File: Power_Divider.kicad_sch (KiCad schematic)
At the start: 28 parts, among them J8 Molex 73251-1153, J9 PIC-S-201F, P10 CONUFL001-SMD-T, P11 CONUFL001-SMD-T, P12 CONUFL001-SMD-T, P9 CONUFL001-SMD-T, U25 QPL9547, U26 RBP-140+

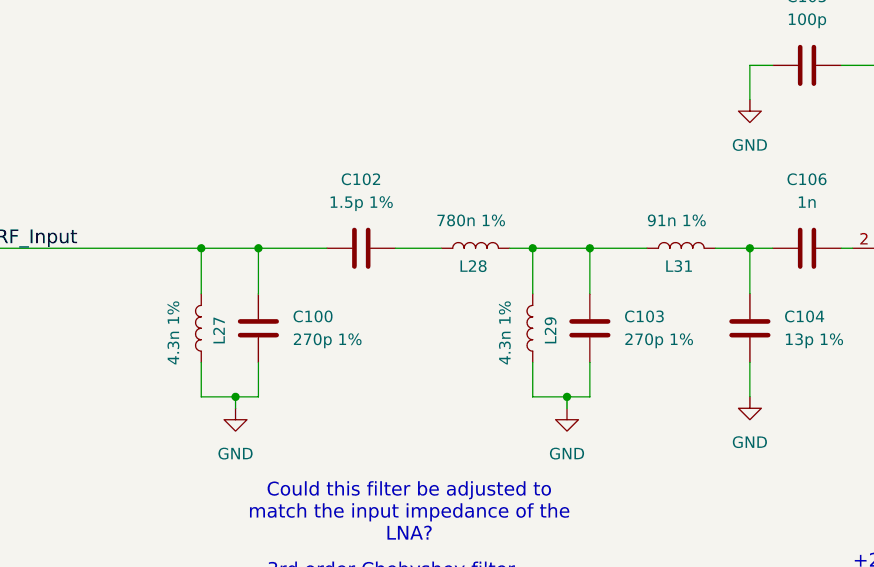
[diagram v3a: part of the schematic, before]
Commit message: More work on the LNA
Rework the filter a bit, rework the layout.

Signed-off-by: Corey Minyard <corey@minyard.net>
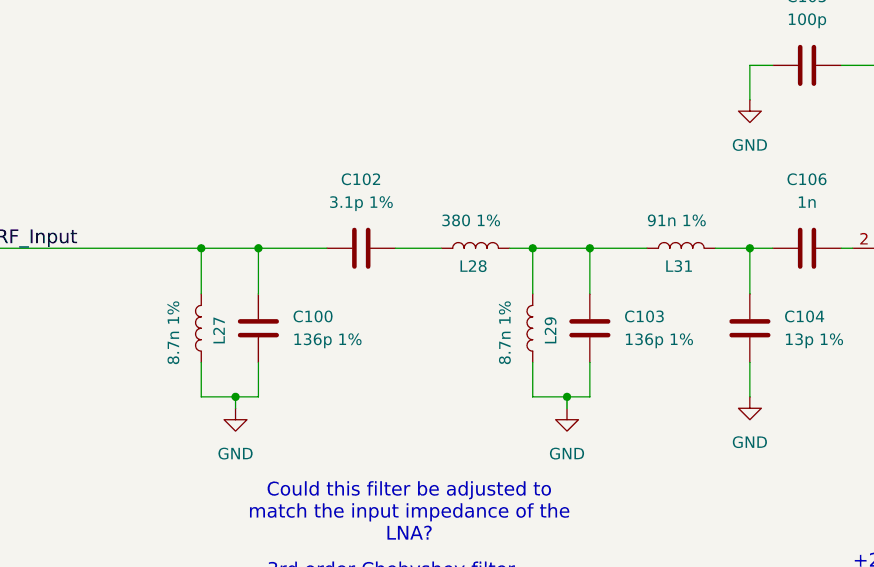
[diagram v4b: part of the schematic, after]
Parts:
- C100, C103: value 270p 1% -> 136p 1%
- C102: value 1.5p 1% -> 3.1p 1%
- L27, L29: value 4.3n 1% -> 8.7n 1%
- L28: value 780n 1% -> 380 1%
- L31: footprint Inductor_SMD:L_0402_1005Metric_Pad0.77x0.64mm_HandSolder -> Inductor_SMD:L_0603_1608Metric_Pad1.05x0.95mm_HandSolder
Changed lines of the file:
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@@
 			)
 		)
-		(property "Footprint" "Inductor_SMD:L_0402_1005Metric_Pad0.77x0.64mm_HandSolder"
+		(property "Footprint" "Inductor_SMD:L_0603_1608Metric_Pad1.05x0.95mm_HandSolder"
 			(at 134.62 143.51 0)
 			(effects
@@
 			)
 		)
-		(property "Value" "270p 1%"
+		(property "Value" "136p 1%"
 			(at 91.44 153.6699 0)
 			(effects
@@
 			)
 		)
-		(property "Value" "4.3n 1%"
+		(property "Value" "8.7n 1%"
 			(at 78.232 152.908 90)
 			(effects
@@
 			)
 		)
-		(property "Value" "780n 1%"
+		(property "Value" "380 1%"
 			(at 111.252 140.462 90)
 			(effects
@@
 			)
 		)
-		(property "Value" "4.3n 1%"
+		(property "Value" "8.7n 1%"
 			(at 115.062 152.908 90)
 			(effects
@@
 			)
 		)
-		(property "Value" "1.5p 1%"
+		(property "Value" "3.1p 1%"
 			(at 99.06 138.43 90)
 			(effects
@@
 			)
 		)
-		(property "Value" "270p 1%"
+		(property "Value" "136p 1%"
 			(at 128.27 153.6699 0)
 			(effects

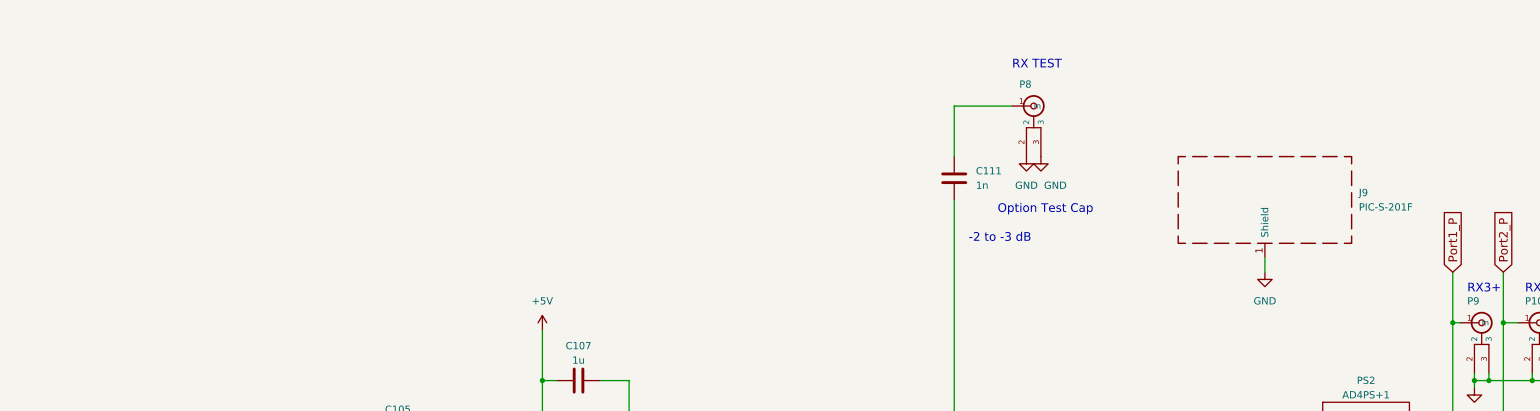
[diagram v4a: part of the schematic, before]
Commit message: Change to aluminum shielding
Signed-off-by: Corey Minyard <corey@minyard.net>
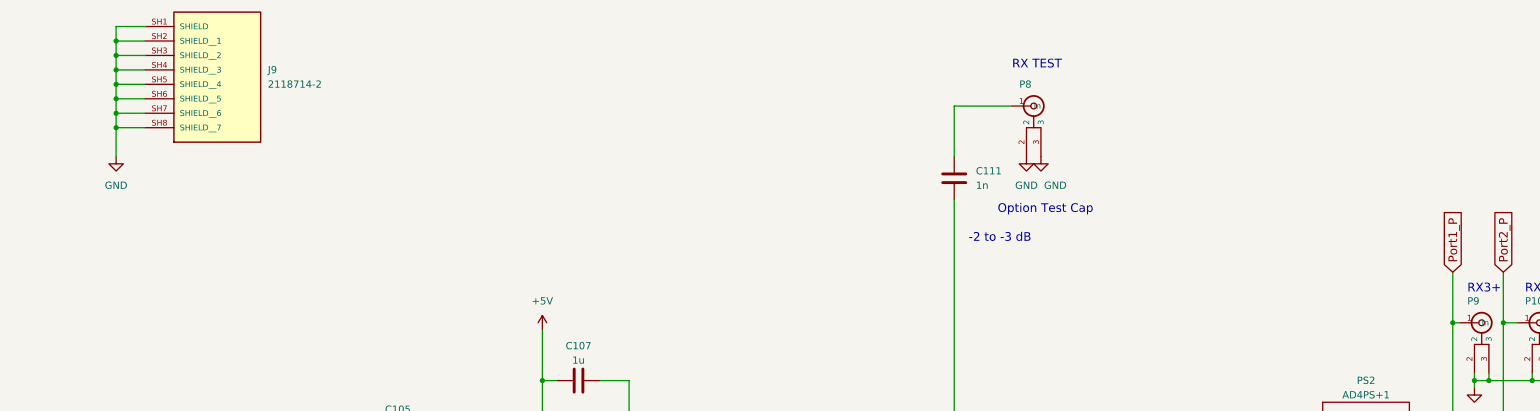
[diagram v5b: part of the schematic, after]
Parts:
- removed J9: PIC-S-201F, PacSatDev_misc:RF_SHIELD_PIC_S_101, symbol Device:RFShield_OnePiece
- added J9: 2118714-2, PacSatDev_misc:TE_2118714-2, symbol PACSAT_DEV_misc:2118714-2
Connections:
- net GND: now also J9.SH1 (SHIELD), J9.SH2 (SHIELD__1), J9.SH3 (SHIELD__2), J9.SH4 (SHIELD__3), J9.SH5 (SHIELD__4), J9.SH6 (SHIELD__5), J9.SH7 (SHIELD__6), J9.SH8 (SHIELD__7)

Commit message: More shield work
Signed-off-by: Corey Minyard <corey@minyard.net>
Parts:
- L28: value 380 1% -> 380n 1%
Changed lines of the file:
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@@
 	(text "3rd order Chebyshev filter\nConventional Shunt First\nPassband 140-152MHz\n.1db ripple in passband\n"
 		(exclude_from_sim no)
-		(at 102.362 183.134 0)
+		(at 101.092 127.254 0)
 		(effects
 			(font
@@
 			)
 		)
-		(property "Value" "380 1%"
+		(property "Value" "380n 1%"
 			(at 111.252 140.462 90)
 			(effects

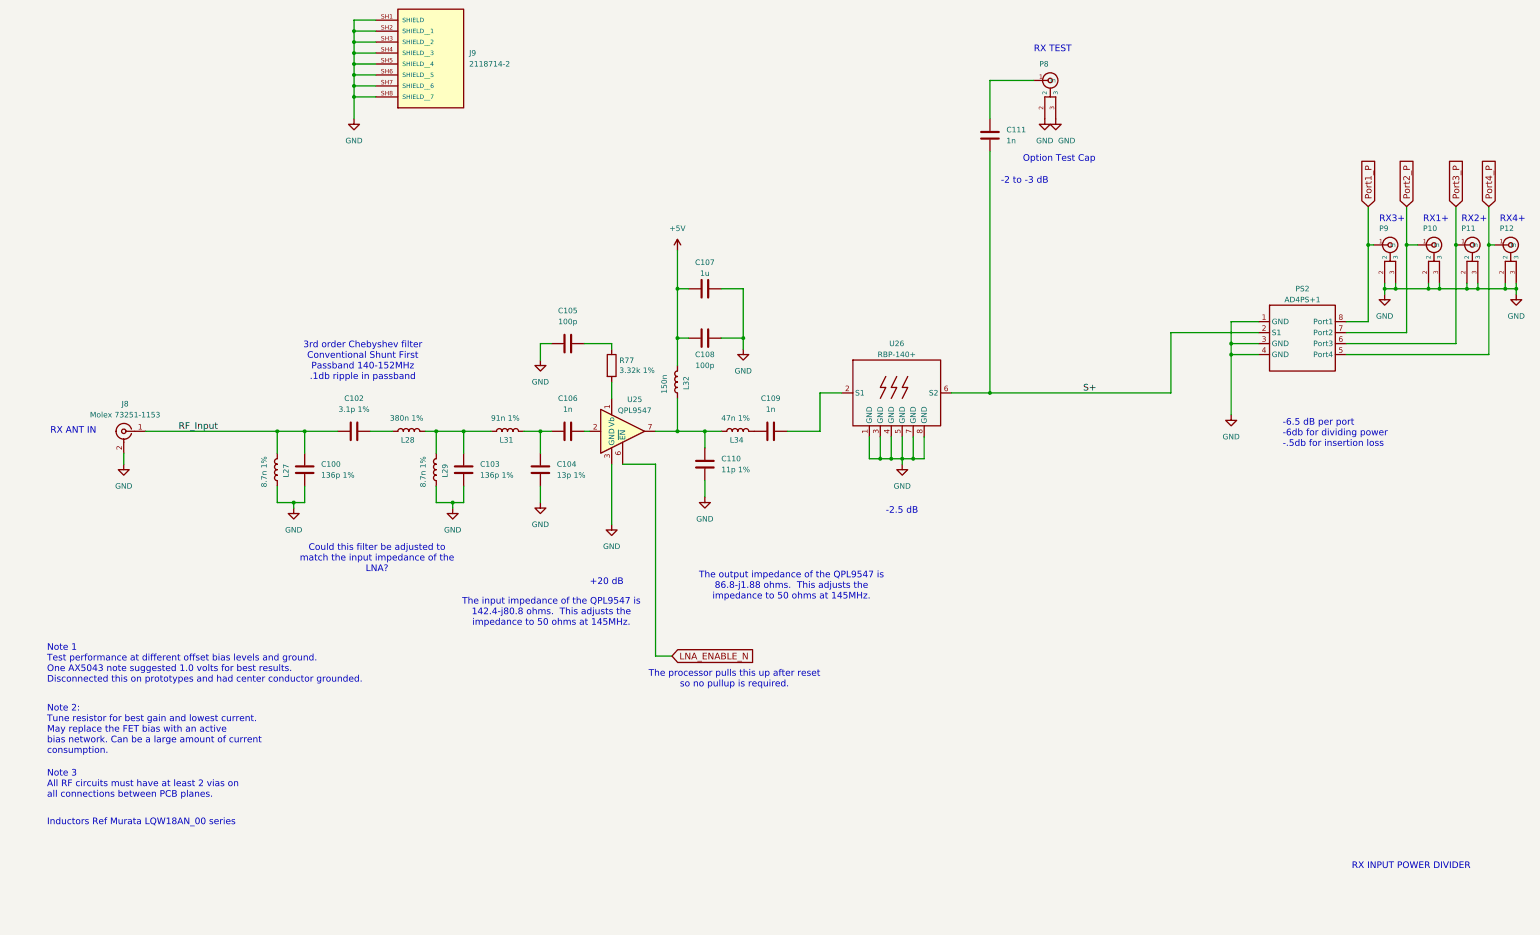
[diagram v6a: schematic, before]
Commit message: Rework the LNA input filter
Some more :(

Signed-off-by: Corey Minyard <corey@minyard.net>
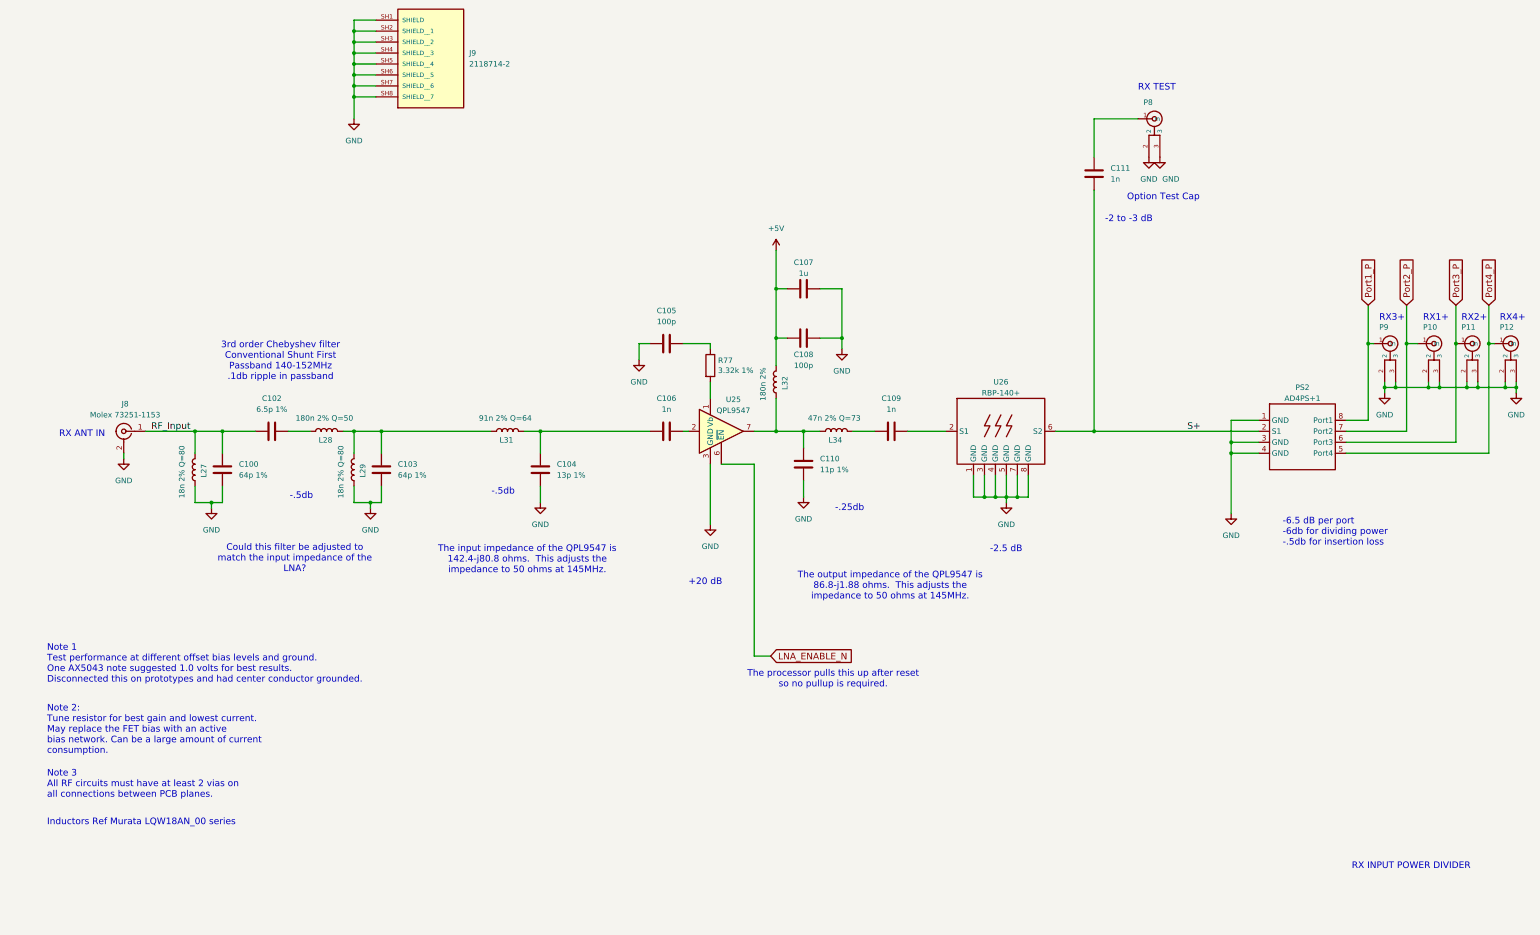
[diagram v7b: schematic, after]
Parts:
- C100, C103: value 136p 1% -> 64p 1%
- C102: value 3.1p 1% -> 6.5p 1%
- L27, L29: value 8.7n 1% -> 18n 2% Q=80
- L28: value 380n 1% -> 180n 2% Q=50; footprint Inductor_SMD:L_0603_1608Metric_Pad1.05x0.95mm_HandSolder -> Inductor_SMD:L_0805_2012Metric
- L31: value 91n 1% -> 91n 2% Q=64
- L32: value 150n -> 180n 2%
- L34: value 47n 1% -> 47n 2% Q=73; footprint Inductor_SMD:L_0402_1005Metric_Pad0.77x0.64mm_HandSolder -> Inductor_SMD:L_0603_1608Metric
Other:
- note added: "-.25db"
- note added: "-.5db"
- moved on the sheet: C100, C102, C103, C105, C106, C107, C108, C109, C110, C111, L27, L28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

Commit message: Lots of work on the documentation
Signed-off-by: Corey Minyard <corey@minyard.net>
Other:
- note added: "All RF capacitors C0G/NP0."
- note removed: "Inductors Ref Murata LQW18AN_00 series"
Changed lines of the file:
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@@
 		)
 	)
-	(text "Inductors Ref Murata LQW18AN_00 series"
+	(text "All RF capacitors C0G/NP0."
 		(exclude_from_sim no)
 		(at 27.94 234.95 0)
